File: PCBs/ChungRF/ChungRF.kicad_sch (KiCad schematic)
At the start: 15 parts, among them J1 Conn_Coaxial, J2 Conn_01x09_Socket, U1 E22-900M30S

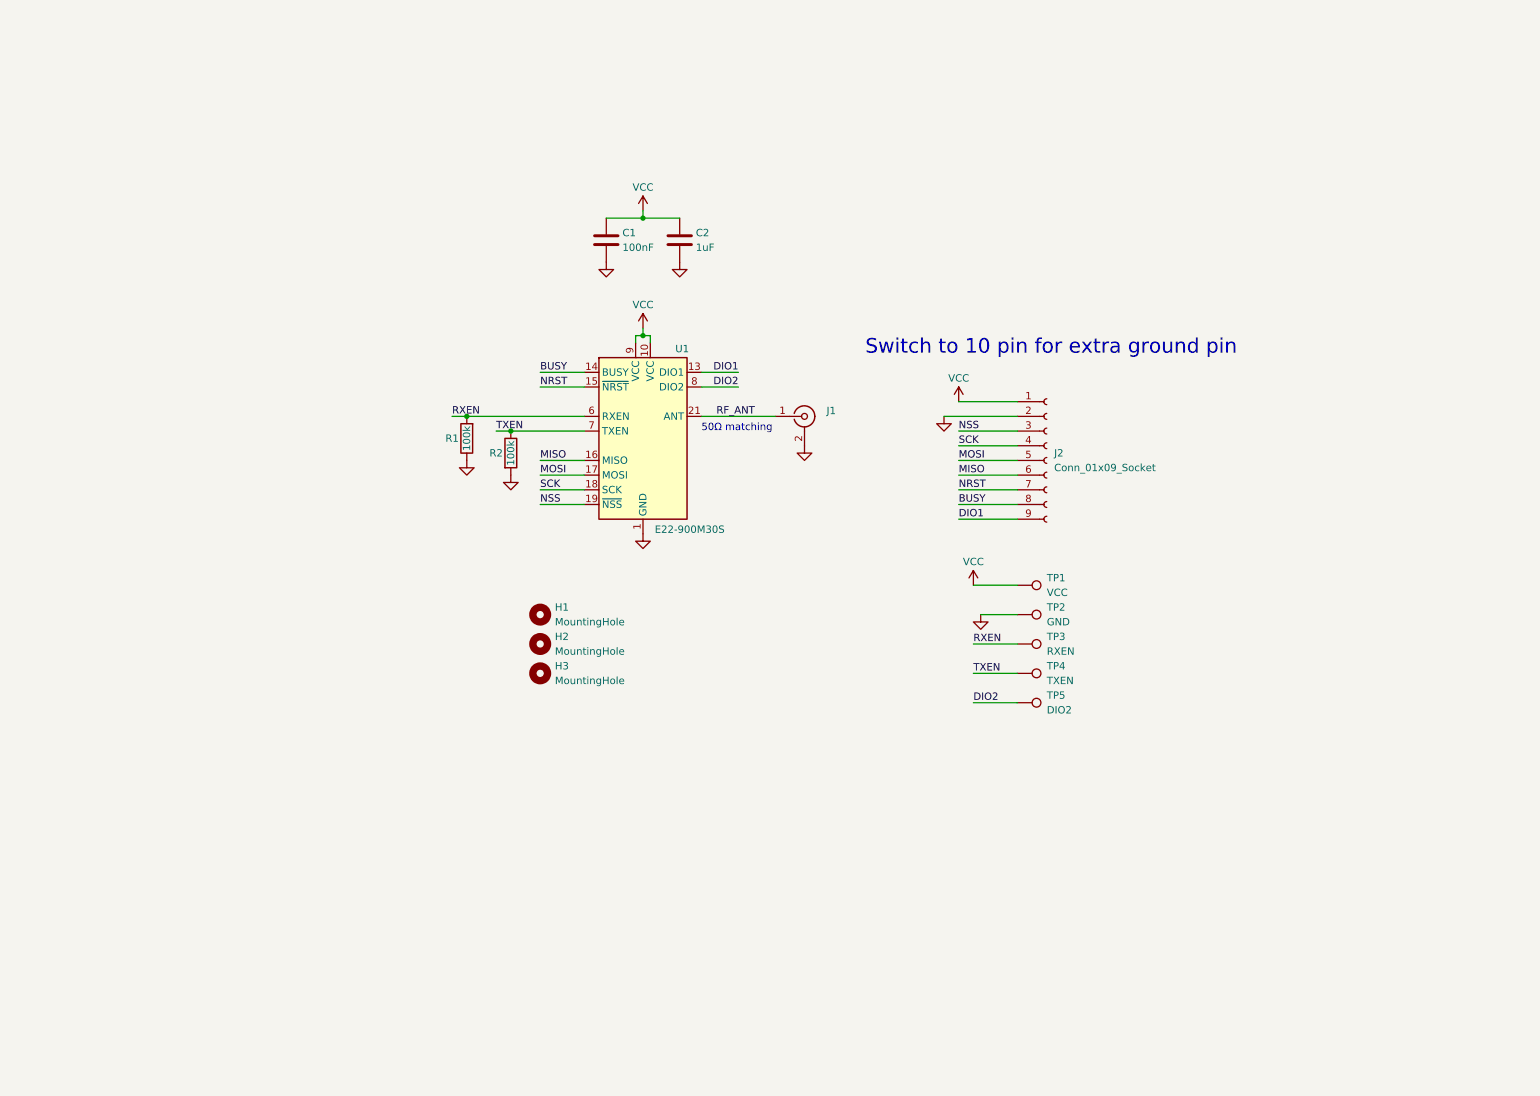
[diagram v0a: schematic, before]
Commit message: Add ESP32-S3-MINI
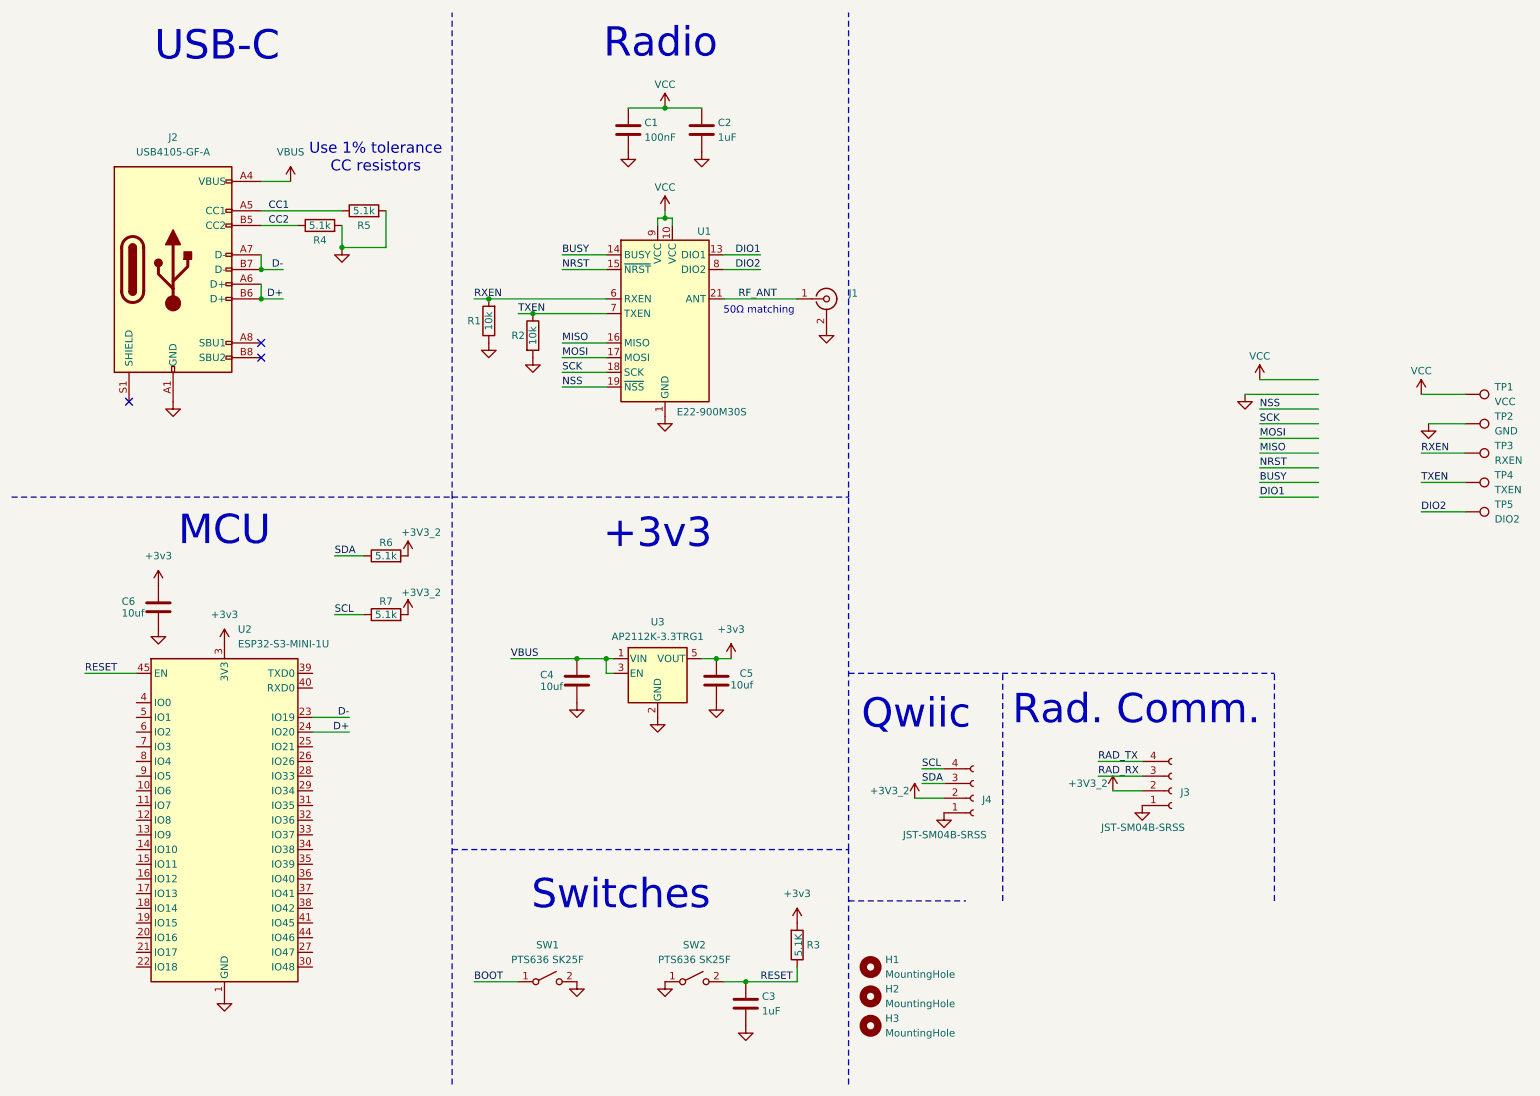
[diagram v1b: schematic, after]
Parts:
- removed J2: Conn_01x09_Socket, Connector_JST:JST_SH_SM09B-SRSS-TB_1x09-1MP_P1.00mm_Horizontal, symbol Connector:Conn_01x09_Socket
- added C3: 1uF, Capacitor_SMD:C_0603_1608Metric, symbol Device:C
- added C4, C5, C6: 10uf, Capacitor_SMD:C_0603_1608Metric, symbol Device:C
- added J2: USB4105-GF-A, Connector_USB:USB_C_Receptacle_GCT_USB4105-xx-A_16P_TopMnt_Horizontal, symbol Connector:USB_C_Receptacle_USB2.0_16P
- added J3, J4: JST-SM04B-SRSS, besser_footprints:JST_SH_SM04B-SRSS-TB_1x04-1MP_P1.00mm_Horizontal, symbol Connector:Conn_01x04_Socket
- added R3: 5.1K, Capacitor_SMD:C_0603_1608Metric, symbol Device:R
- added R4, R5, R6, R7: 5.1k, Capacitor_SMD:C_0603_1608Metric, symbol Device:R
- added SW1, SW2: PTS636 SK25F, Button_Switch_SMD:SW_Tactile_SPST_NO_Straight_CK_PTS636Sx25SMTRLFS, symbol Switch:SW_SPST
- added U2: ESP32-S3-MINI-1U, RF_Module:ESP32-S2-MINI-1U, symbol RF_Module:ESP32-S3-MINI-1U
- added U3: AP2112K-3.3TRG1, Package_TO_SOT_SMD:SOT-23-5, symbol Regulator_Linear:AP2112K-3.3
- R1, R2: value 100k -> 10k
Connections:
- net GND: now also C3.2, C4.1, C5.2, C6.1, J2.A1 (GND), J2.A12 (GND), J2.B1 (GND), J2.B12 (GND), J3.1 (Pin_1), J4.1 (Pin_1), R4.2, R5.2, SW1.2 (B), SW2.1 (A), U2.1 (GND), U2.2 (GND), U2.42 (GND), U2.43 (GND), U2.46 (GND), U2.47 (GND), U2.48 (GND), U2.49 (GND), U2.50 (GND), U2.51 (GND), U2.52 (GND), U2.53 (GND), U2.54 (GND), U2.55 (GND), U2.56 (GND), U2.57 (GND), U2.58 (GND), U2.59 (GND), U2.60 (GND), U2.61 (GND), U2.62 (GND), U2.63 (GND), U2.64 (GND), U2.65 (GND), U3.2 (GND)
- new net +3V3_2: J3.2 (Pin_2), J4.2 (Pin_2), R6.2, R7.2
- new net +3v3: C5.1, C6.2, R3.2, U2.3 (3V3), U3.5 (VOUT)
- new net BOOT: SW1.1 (A)
- new net CC1: J2.A5 (CC1), R5.1
- new net CC2: J2.B5 (CC2), R4.1
- new net D+: J2.A6 (D+), J2.B6 (D+), U2.24 (IO20)
- new net D-: J2.A7 (D-), J2.B7 (D-), U2.23 (IO19)
- new net RAD_RX: J3.3 (Pin_3)
- new net RAD_TX: J3.4 (Pin_4)
- new net RESET: C3.1, R3.1, SW2.2 (B), U2.45 (EN)
- new net SCL: J4.4 (Pin_4), R7.1
- new net SDA: J4.3 (Pin_3), R6.1
- new net VBUS: C4.2, J2.A4 (VBUS), J2.A9 (VBUS), J2.B4 (VBUS), J2.B9 (VBUS), U3.1 (VIN), U3.3 (EN)
- no-connect marks 0 -> 3
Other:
- note added: "+3v3"
- note added: "MCU"
- note added: "Qwiic"
- note added: "Rad. Comm."
- note added: "Radio"
- note added: "Switches"
- note added: "USB-C"
- note added: "Use 1% tolerance CC resistors"
- note removed: "Switch to 10 pin for extra ground pin"
- moved on the sheet: C1, C2, H1, H2, H3, J1, R1, R2, TP1, TP2, TP3, TP4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

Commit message: ChungRF R2
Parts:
- removed C4, C5, C6: 10uf, Capacitor_SMD:C_0603_1608Metric, symbol Device:C
- removed H3: MountingHole, MountingHole:MountingHole_2.7mm_M2.5_Pad_Via, symbol Mechanical:MountingHole
- removed J2: USB4105-GF-A, Connector_USB:USB_C_Receptacle_GCT_USB4105-xx-A_16P_TopMnt_Horizontal, symbol Connector:USB_C_Receptacle_USB2.0_16P
- removed J4: JST-SM04B-SRSS, besser_footprints:JST_SH_SM04B-SRSS-TB_1x04-1MP_P1.00mm_Horizontal, symbol Connector:Conn_01x04_Socket
- removed R3: 5.1K, Capacitor_SMD:C_0603_1608Metric, symbol Device:R
- removed R4, R5, R6, R7: 5.1k, Capacitor_SMD:C_0603_1608Metric, symbol Device:R
- removed SW1, SW2: PTS636 SK25F, Button_Switch_SMD:SW_Tactile_SPST_NO_Straight_CK_PTS636Sx25SMTRLFS, symbol Switch:SW_SPST
- removed TP1: VCC, TestPoint:TestPoint_Pad_D1.5mm, symbol Connector:TestPoint
- removed TP2: GND, TestPoint:TestPoint_Pad_D1.5mm, symbol Connector:TestPoint
- removed TP3: RXEN, TestPoint:TestPoint_Pad_D1.5mm, symbol Connector:TestPoint
- removed TP4: TXEN, TestPoint:TestPoint_Pad_D1.5mm, symbol Connector:TestPoint
- removed TP5: DIO2, TestPoint:TestPoint_Pad_D1.5mm, symbol Connector:TestPoint
- removed U2: ESP32-S3-MINI-1U, RF_Module:ESP32-S2-MINI-1U, symbol RF_Module:ESP32-S3-MINI-1U
- removed U3: AP2112K-3.3TRG1, Package_TO_SOT_SMD:SOT-23-5, symbol Regulator_Linear:AP2112K-3.3
- added U1: KB2040, besser_footprints:Adafuit-KB2040-SMD, symbol besserLib:Adafruit-KB2040
- C3: value 1uF -> 10uF
- H1, H2: value MountingHole -> 2.7mm_M2.5_Pad_Via
- J2: renamed from J1; footprint besser_footprints:CON-SMA-EDGE-S -> besser_footprints:CONSMA003.062
- renumbered J3 to J1, U1 to U2
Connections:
- net +3V3_2 is gone; now on net VBUS: J1.2 (Pin_2)
- net RESET is gone; now on net VBUS: C3.1
- net VCC is gone; now on net VBUS: C1.1, C2.1, U2.10 (VCC), U2.9 (VCC)
- net BUSY: now also U1.19 (A1)
- net DIO1: now also U1.20 (A2)
- net DIO2: now also U1.7 (D3)
- net GND: now also U1.24 (GND), U1.4 (GND), U1.5 (GND)
- net MISO: now also U1.17 (SCK)
- net MOSI: now also U1.16 (MISO)
- net NRST: now also U1.18 (A0)
- net NSS: now also U1.14 (D10)
- net SCK: now also U1.15 (MOSI)
- net VBUS: now also U1.25 (RAW)
- net RAD_RX renamed CARFIO_MISO
- net CARFIO_MISO: now also U1.3 (D1)
- net RAD_TX renamed CARFIO_MOSI
- net CARFIO_MOSI: now also U1.2 (D0)
- no-connect marks 3 -> 12
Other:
- note added: "IO Conn."
- note added: "No protection against USB and CARFIO power. Only plug one in at a time."
- note added: "Pins connections do not follow convention for easier routing."
- note removed: "+3v3"
- note removed: "Qwiic"
- note removed: "Rad. Comm."
- note removed: "Switches"
- note removed: "USB-C"
- note removed: "Use 1% tolerance CC resistors"
- moved on the sheet: C1, C2, J1
